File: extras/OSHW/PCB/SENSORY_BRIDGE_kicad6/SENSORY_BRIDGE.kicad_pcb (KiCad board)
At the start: 2 copper layers, 70 x 70 mm, 44 parts, among them IC1 ESP32-S2-MINI-1-N4R2, J1 USB4110-GF-A_REVB, J2 796949-4, SW1 1825910-6, SW2 1825910-6, SW3 PTS525SM15SMTR2LFS, SW4 PTS525SM15SMTR2LFS, U1 SPH0645LM4H-B, U2 AZ1117-3.3, U3 ECMF02-4CMX8

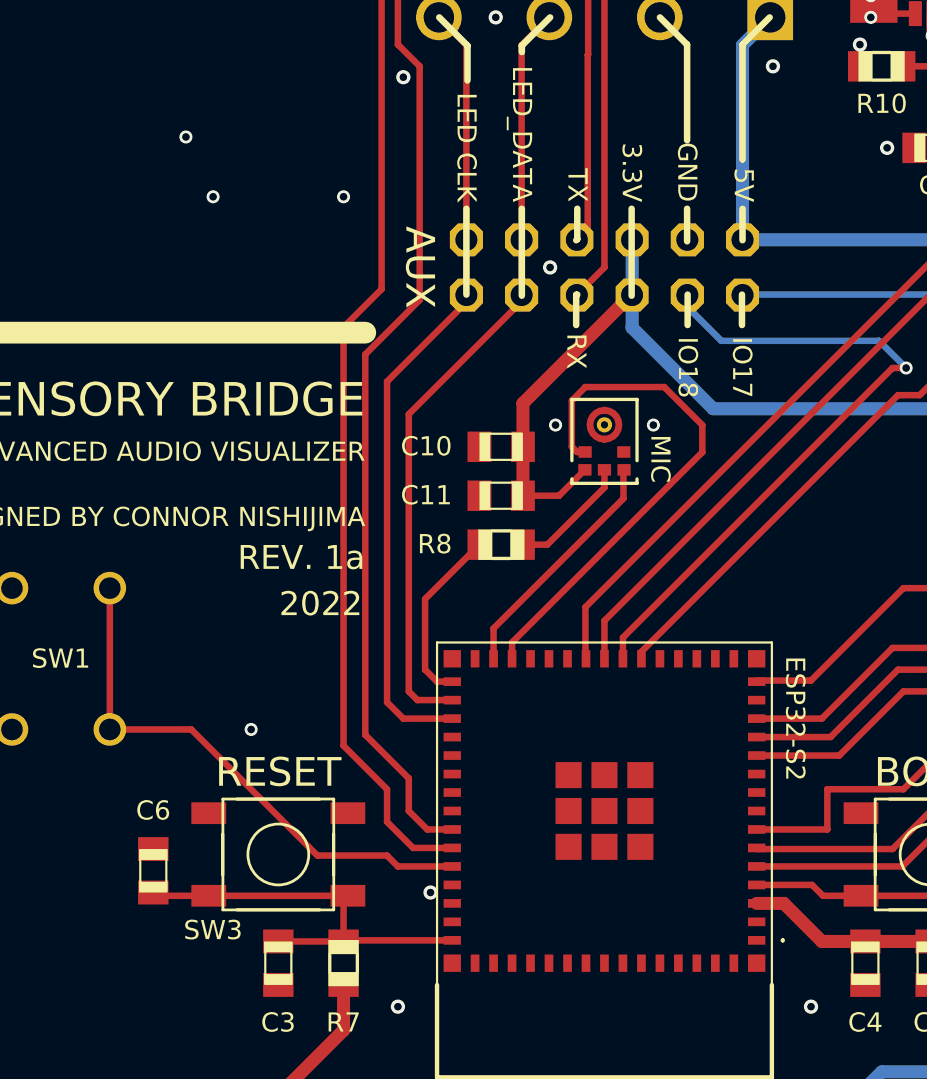
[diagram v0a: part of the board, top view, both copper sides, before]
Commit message: Fixed pads for mems microphone and mounting holes
Also added BOM
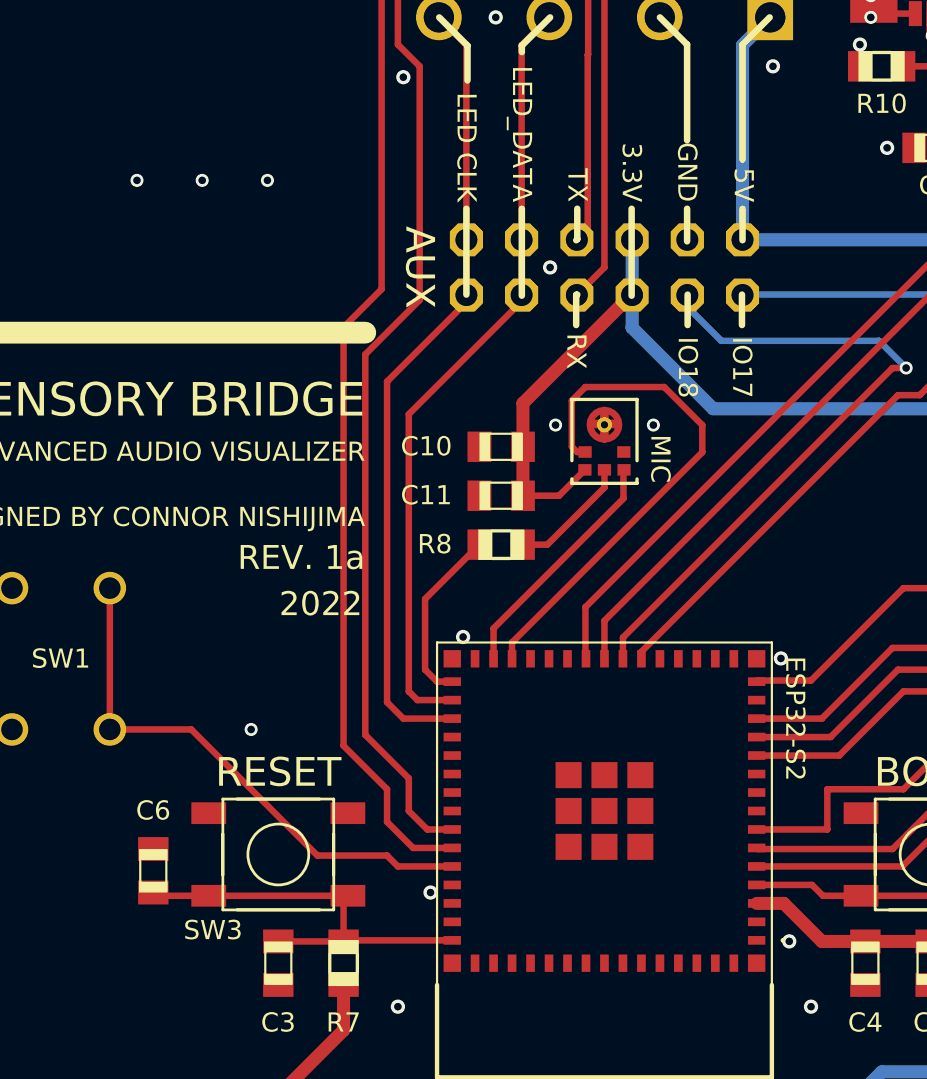
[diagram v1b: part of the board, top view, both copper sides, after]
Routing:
- net /GND: vias 144 -> 147
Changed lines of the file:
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@@
       (connect_pads (clearance 0))
       (min_thickness 0.254)
-      (keepout (tracks not_allowed) (vias not_allowed) (pads not_allowed ) (copperpour not_allowed) (footprints allowed))
+      (keepout (tracks not_allowed) (vias not_allowed) (pads not_allowed) (copperpour not_allowed) (footprints allowed))
       (fill (thermal_gap 0.508) (thermal_bridge_width 0.508))
       (polygon
@@
       (connect_pads (clearance 0))
       (min_thickness 0.254)
-      (keepout (tracks not_allowed) (vias not_allowed) (pads not_allowed ) (copperpour not_allowed) (footprints allowed))
+      (keepout (tracks not_allowed) (vias not_allowed) (pads not_allowed) (copperpour not_allowed) (footprints allowed))
       (fill (thermal_gap 0.508) (thermal_bridge_width 0.508))
       (polygon
@@
       (connect_pads (clearance 0))
       (min_thickness 0.254)
-      (keepout (tracks not_allowed) (vias not_allowed) (pads not_allowed ) (copperpour not_allowed) (footprints allowed))
+      (keepout (tracks not_allowed) (vias not_allowed) (pads not_allowed) (copperpour not_allowed) (footprints allowed))
       (fill (thermal_gap 0.508) (thermal_bridge_width 0.508))
       (polygon
@@
       (connect_pads (clearance 0))
       (min_thickness 0.254)
-      (keepout (tracks not_allowed) (vias not_allowed) (pads not_allowed ) (copperpour not_allowed) (footprints allowed))
+      (keepout (tracks not_allowed) (vias not_allowed) (pads not_allowed) (copperpour not_allowed) (footprints allowed))
       (fill (thermal_gap 0.508) (thermal_bridge_width 0.508))
       (polygon
@@
     (fp_arc (start 1.1708 -0.9756) (mid 1.432981 -0.518783) (end 1.524 0) (layer "B.SilkS") (width 0.1524))
     (fp_arc (start 0 -2.032) (mid 0.854953 -1.843405) (end 1.5512 -1.3126) (layer "B.SilkS") (width 0.254))
-    (fp_arc (start -1.7891 0.9634) (mid -1.970339 0.496774) (end -2.032 0) (layer "B.SilkS") (width 0.254))
+    (fp_arc (start -1.7891 0.9634) (mid -1.970338 0.496774) (end -2.032 0) (layer "B.SilkS") (width 0.254))
     (fp_arc (start 0 -1.524) (mid 0.669593 -1.369018) (end 1.203 -0.9356) (layer "B.SilkS") (width 0.1524))
     (fp_arc (start 0 2.032) (mid -1.045438 1.7424) (end -1.7929 0.9562) (layer "B.SilkS") (width 0.254))
     (fp_arc (start 1.524 0) (mid 1.429332 0.528743) (end 1.1571 0.9918) (layer "B.SilkS") (width 0.1524))
-    (fp_arc (start -1.1708 0.9756) (mid -1.432981 0.518783) (end -1.524 0) (layer "B.SilkS") (width 0.1524))
+    (fp_arc (start -1.1708 0.9756) (mid -1.43298 0.518783) (end -1.524 0) (layer "B.SilkS") (width 0.1524))
     (fp_arc (start 1.2401 0.885801) (mid 0.697339 1.355082) (end 0 1.524) (layer "B.SilkS") (width 0.1524))
     (fp_arc (start -1.203 -0.9356) (mid -0.669593 -1.369018) (end 0 -1.524) (layer "B.SilkS") (width 0.1524))
@@
     (fp_arc (start 0 -2.032) (mid 0.854953 -1.843405) (end 1.5512 -1.3126) (layer "B.SilkS") (width 0.254))
     (fp_arc (start 1.2401 0.885801) (mid 0.697339 1.355082) (end 0 1.524) (layer "B.SilkS") (width 0.1524))
-    (fp_arc (start -1.7891 0.9634) (mid -1.970339 0.496774) (end -2.032 0) (layer "B.SilkS") (width 0.254))
-    (fp_arc (start -1.1708 0.9756) (mid -1.432981 0.518783) (end -1.524 0) (layer "B.SilkS") (width 0.1524))
+    (fp_arc (start -1.7891 0.9634) (mid -1.970338 0.496774) (end -2.032 0) (layer "B.SilkS") (width 0.254))
+    (fp_arc (start -1.1708 0.9756) (mid -1.43298 0.518783) (end -1.524 0) (layer "B.SilkS") (width 0.1524))
     (fp_arc (start -1.7643 -1.0082) (mid -1.019924 -1.757525) (end 0 -2.032) (layer "B.SilkS") (width 0.254))
     (fp_arc (start 1.524 0) (mid 1.429332 0.528743) (end 1.1571 0.9918) (layer "B.SilkS") (width 0.1524))
@@
     (fp_arc (start 1.2401 0.885801) (mid 0.697339 1.355082) (end 0 1.524) (layer "B.SilkS") (width 0.1524))
     (fp_arc (start 1.561 1.3009) (mid 0.861864 1.840173) (end 0 2.032) (layer "B.SilkS") (width 0.254))
-    (fp_arc (start -1.7891 0.9634) (mid -1.970339 0.496774) (end -2.032 0) (layer "B.SilkS") (width 0.254))
+    (fp_arc (start -1.7891 0.9634) (mid -1.970338 0.496774) (end -2.032 0) (layer "B.SilkS") (width 0.254))
     (fp_arc (start -2.032 0) (mid -1.95521 -0.553417) (end -1.7306 -1.065) (layer "B.SilkS") (width 0.254))
     (fp_arc (start -1.524 0) (mid -1.42454 -0.5416) (end -1.1391 -1.0125) (layer "B.SilkS") (width 0.1524))
     (fp_arc (start -1.7643 -1.0082) (mid -1.019924 -1.757525) (end 0 -2.032) (layer "B.SilkS") (width 0.254))
-    (fp_arc (start -1.1708 0.9756) (mid -1.432981 0.518783) (end -1.524 0) (layer "B.SilkS") (width 0.1524))
+    (fp_arc (start -1.1708 0.9756) (mid -1.43298 0.518783) (end -1.524 0) (layer "B.SilkS") (width 0.1524))
     (fp_arc (start 0 1.016) (mid -0.71842 0.71842) (end -1.016 0) (layer "B.Fab") (width 0.1524))
     (fp_arc (start 0 0.635) (mid -0.449013 0.449013) (end -0.635 0) (layer "B.Fab") (width 0.1524))
@@
       (net 2 "/GND") (pinfunction "4") (pintype "passive") (solder_mask_margin 0.0508))
   )
+  (gr_rect (start 147.9 94.1) (end 149.1 94.3) (layer "F.Cu") (width 0.2) (fill solid))
+  (gr_rect (start 148.4 93.6) (end 148.6 94.9) (layer "F.Cu") (width 0.2) (fill solid))
   (gr_line (start 152.3011 76.7536) (end 152.3011 81.1536) (layer "F.SilkS") (width 0.3))
   (gr_line (start 142.1511 84.3036) (end 142.1511 88.2536) (layer "F.SilkS") (width 0.3))
@@
   (gr_line (start 113.5011 90.0036) (end 137.5011 90.0036) (layer "F.SilkS") (width 1))
   (gr_line (start 147.2011 88.3036) (end 147.2511 88.2536) (layer "F.SilkS") (width 0.3))
-  (gr_circle (center 118.5011 135.0036) (end 121.5011 135.0036) (layer "B.Mask") (width 0.1) (fill none))
-  (gr_circle (center 178.5011 75.0036) (end 181.5011 75.0036) (layer "B.Mask") (width 0.1) (fill none))
-  (gr_circle (center 118.5011 75.0036) (end 121.5011 75.0036) (layer "B.Mask") (width 0.1) (fill none))
-  (gr_circle (center 178.5011 135.0036) (end 181.5011 135.0036) (layer "B.Mask") (width 0.1) (fill none))
+  (gr_circle (center 118.5011 135.0036) (end 121.5011 135.0036) (layer "B.Mask") (width 0.1) (fill solid))
+  (gr_circle (center 178.5011 75.0036) (end 181.5011 75.0036) (layer "B.Mask") (width 0.1) (fill solid))
+  (gr_circle (center 118.5011 75.0036) (end 121.5011 75.0036) (layer "B.Mask") (width 0.1) (fill solid))
+  (gr_circle (center 178.5011 135.0036) (end 181.5011 135.0036) (layer "B.Mask") (width 0.1) (fill solid))
   (gr_line (start 113.5011 70.0036) (end 113.5011 140.0036) (layer "Edge.Cuts") (width 0.001))
   (gr_line (start 113.5011 140.0036) (end 183.5011 140.0036) (layer "Edge.Cuts") (width 0.001))
@@
   (via (at 114.5011 133.0036) (size 0.6548) (drill 0.35) (layers "F.Cu" "B.Cu") (net 2))
   (via (at 182.5011 101.0036) (size 0.6548) (drill 0.35) (layers "F.Cu" "B.Cu") (net 2))
+  (via (at 157 118) (size 0.6548) (drill 0.35) (layers "F.Cu" "B.Cu") (net 2))
   (via (at 182.5011 89.0036) (size 0.6548) (drill 0.35) (layers "F.Cu" "B.Cu") (net 2))
   (via (at 146.5011 71.0036) (size 0.6548) (drill 0.35) (layers "F.Cu" "B.Cu") (net 2))
@@
   (via (at 160.7511 74.5036) (size 0.6) (drill 0.35) (layers "F.Cu" "B.Cu") (net 2))
   (via (at 128.5011 71.0036) (size 0.6548) (drill 0.35) (layers "F.Cu" "B.Cu") (net 2))
+  (via (at 156.617116 104.986852) (size 0.6548) (drill 0.35) (layers "F.Cu" "B.Cu") (net 2))
   (via (at 114.5011 105.0036) (size 0.6548) (drill 0.35) (layers "F.Cu" "B.Cu") (net 2))
   (via (at 152.5011 71.0036) (size 0.6548) (drill 0.35) (layers "F.Cu" "B.Cu") (net 2))
@@
   (via (at 171.2511 74.5036) (size 0.6) (drill 0.35) (layers "F.Cu" "B.Cu") (net 2))
   (via (at 182.5011 111.0036) (size 0.6548) (drill 0.35) (layers "F.Cu" "B.Cu") (net 2))
-  (via (at 129.2511 81.0036) (size 0.6) (drill 0.35) (layers "F.Cu" "B.Cu") (net 2))
+  (via (at 127 83) (size 0.6) (drill 0.35) (layers "F.Cu" "B.Cu") (net 2))
   (via (at 170.0011 76.7536) (size 0.6548) (drill 0.35) (layers "F.Cu" "B.Cu") (net 2))
   (via (at 132.5011 71.0036) (size 0.6548) (drill 0.35) (layers "F.Cu" "B.Cu") (net 2))
@@
   (via (at 114.5011 129.0036) (size 0.6548) (drill 0.35) (layers "F.Cu" "B.Cu") (net 2))
   (via (at 114.5011 109.0036) (size 0.6548) (drill 0.35) (layers "F.Cu" "B.Cu") (net 2))
-  (via (at 136.5011 83.7536) (size 0.6) (drill 0.35) (layers "F.Cu" "B.Cu") (net 2))
+  (via (at 133 83) (size 0.6) (drill 0.35) (layers "F.Cu" "B.Cu") (net 2))
   (via (at 174.5011 139.0036) (size 0.6548) (drill 0.35) (layers "F.Cu" "B.Cu") (net 2))
   (via (at 114.5011 85.0036) (size 0.6548) (drill 0.35) (layers "F.Cu" "B.Cu") (net 2))
@@
   (via (at 182.5011 107.0036) (size 0.6548) (drill 0.35) (layers "F.Cu" "B.Cu") (net 2))
   (via (at 182.5011 79.0036) (size 0.6548) (drill 0.35) (layers "F.Cu" "B.Cu") (net 2))
-  (via (at 130.5011 83.7536) (size 0.6) (drill 0.35) (layers "F.Cu" "B.Cu") (net 2))
+  (via (at 130 83) (size 0.6) (drill 0.35) (layers "F.Cu" "B.Cu") (net 2))
   (via (at 160.5011 139.0036) (size 0.6548) (drill 0.35) (layers "F.Cu" "B.Cu") (net 2))
   (via (at 132.2511 108.2536) (size 0.6) (drill 0.35) (layers "F.Cu" "B.Cu") (net 2))
@@
   (via (at 146.0011 87.0036) (size 0.6548) (drill 0.35) (layers "F.Cu" "B.Cu") (net 2))
   (via (at 114.5011 91.0036) (size 0.6548) (drill 0.35) (layers "F.Cu" "B.Cu") (net 2))
+  (via (at 142 104) (size 0.6548) (drill 0.35) (layers "F.Cu" "B.Cu") (net 2))
   (via (at 114.5011 119.0036) (size 0.6548) (drill 0.35) (layers "F.Cu" "B.Cu") (net 2))
   (via (at 182.5011 91.0036) (size 0.6548) (drill 0.35) (layers "F.Cu" "B.Cu") (net 2))
@@
     (connect_pads (clearance 0))
     (min_thickness 0.254)
-    (keepout (tracks not_allowed) (vias not_allowed) (pads not_allowed ) (copperpour not_allowed) (footprints allowed))
+    (keepout (tracks not_allowed) (vias not_allowed) (pads not_allowed) (copperpour not_allowed) (footprints allowed))
     (fill (thermal_gap 0.508) (thermal_bridge_width 0.508))
     (polygon
